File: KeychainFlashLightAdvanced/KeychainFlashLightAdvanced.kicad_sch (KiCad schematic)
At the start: 4 parts, among them SW1 SW_DPST_x2

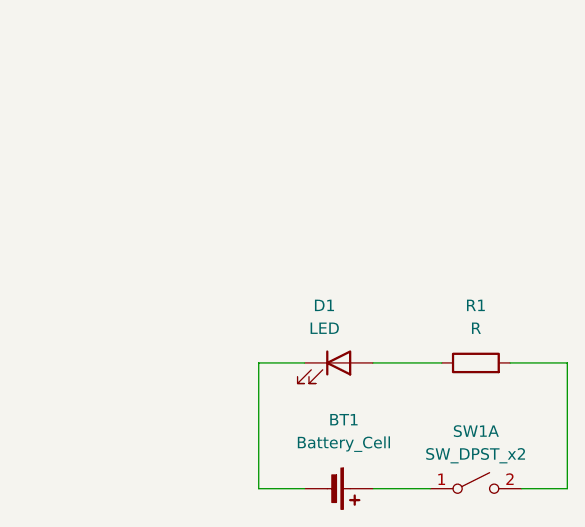
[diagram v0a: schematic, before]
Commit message: Added workshop components
-Add information to the schematic page
-Add informative text to the schematic sheet
-Adding a hierarchical sheet
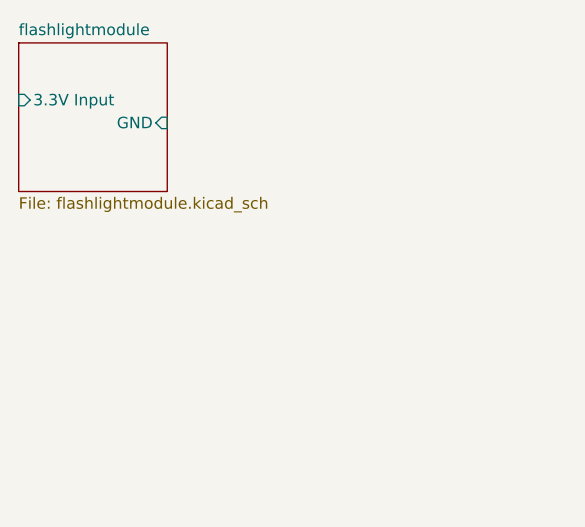
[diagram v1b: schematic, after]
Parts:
- removed BT1: Battery_Cell, Battery:BatteryHolder_Keystone_3002_1x2032, symbol Device:Battery_Cell
- removed D1: LED, LED_THT:LED_D5.0mm_Clear, symbol Device:LED
- removed R1: R, Resistor_THT:R_Axial_DIN0207_L6.3mm_D2.5mm_P10.16mm_Horizontal, symbol Device:R
- removed SW1: SW_DPST_x2, Button_Switch_THT:SW_Tactile_Straight_KSA0Axx1LFTR, symbol Switch:SW_DPST_x2
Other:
- added sheet flashlightmodule (flashlightmodule.kicad_sch)
- title: (none) -> KeychainFlashlightAdvanced
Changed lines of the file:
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@@
 (kicad_sch (version 20230121) (generator eeschema)
-  (paper "A4")
-  (wire (pts (xy 148.59 91.44) (xy 154.94 91.44))
-    (stroke (width 0) (type default))
+  (paper "A5")
+  (title_block
+    (title "KeychainFlashlightAdvanced")
+    (date "2023-12-30")
+    (rev "V0.1")
+    (comment 1 "Made By: Casper Tak")
   )
-  (wire (pts (xy 120.65 91.44) (xy 120.65 105.41))
-    (stroke (width 0) (type default))
-  )
-  (wire (pts (xy 133.35 105.41) (xy 139.7 105.41))
-    (stroke (width 0) (type default))
-  )
-  (wire (pts (xy 154.94 105.41) (xy 149.86 105.41))
-    (stroke (width 0) (type default))
-  )
-  (wire (pts (xy 125.73 91.44) (xy 120.65 91.44))
-    (stroke (width 0) (type default))
-  )
-  (wire (pts (xy 154.94 91.44) (xy 154.94 105.41))
-    (stroke (width 0) (type default))
-  )
-  (wire (pts (xy 133.35 91.44) (xy 140.97 91.44))
-    (stroke (width 0) (type default))
-  )
-  (wire (pts (xy 120.65 105.41) (xy 125.73 105.41))
-    (stroke (width 0) (type default))
-  )
-  (symbol (lib_id "Switch:SW_DPST_x2") (at 144.78 105.41 0) (unit 1)
-    (in_bom yes) (on_board yes) (dnp no) (fields_autoplaced)
-    (property "Reference" "SW1" (at 144.78 99.06 0)
-      (effects (font (size 1.27 1.27)))
+  (sheet (at 93.98 55.88) (size 16.51 16.51) (fields_autoplaced)
+    (stroke (width 0.1524) (type solid))
+    (fill (color 0 0 0 0.0000))
+    (property "Sheetname" "flashlightmodule" (at 93.98 55.1684 0)
+      (effects (font (size 1.27 1.27)) (justify left bottom))
     )
-    (property "Value" "SW_DPST_x2" (at 144.78 101.6 0)
-      (effects (font (size 1.27 1.27)))
+    (property "Sheetfile" "flashlightmodule.kicad_sch" (at 93.98 72.9746 0)
+      (effects (font (size 1.27 1.27)) (justify left top))
     )
-    (property "Footprint" "Button_Switch_THT:SW_Tactile_Straight_KSA0Axx1LFTR" (at 144.78 105.41 0)
-      (effects (font (size 1.27 1.27)) hide)
+    (pin "GND" input (at 110.49 64.77 0)
+      (effects (font (size 1.27 1.27)) (justify right))
     )
-    (property "Datasheet" "~" (at 144.78 105.41 0)
-      (effects (font (size 1.27 1.27)) hide)
+    (pin "3.3V Input" input (at 93.98 62.23 180)
+      (effects (font (size 1.27 1.27)) (justify left))
     )
-    (pin "1")
-    (pin "2")
-    (pin "3")
-    (pin "4")
     (instances
-      (project "KeychainFlashLight"
-        (path "/30398b8a-8fed-4ca8-b3cc-b1f61d914000"
-          (reference "SW1") (unit 1)
-        )
+      (project "KeychainFlashLightAdvanced"
+        (path "/30398b8a-8fed-4ca8-b3cc-b1f61d914000" (page "2"))
       )
     )
-  )
-  (symbol (lib_id "Device:R") (at 144.78 91.44 90) (unit 1)
-    (in_bom yes) (on_board yes) (dnp no) (fields_autoplaced)
-    (property "Reference" "R1" (at 144.78 85.09 90)
-      (effects (font (size 1.27 1.27)))
-    )
-    (property "Value" "R" (at 144.78 87.63 90)
-      (effects (font (size 1.27 1.27)))
-    )
-    (property "Footprint" "Resistor_THT:R_Axial_DIN0207_L6.3mm_D2.5mm_P10.16mm_Horizontal" (at 144.78 93.218 90)
-      (effects (font (size 1.27 1.27)) hide)
-    )
-    (property "Datasheet" "~" (at 144.78 91.44 0)
-      (effects (font (size 1.27 1.27)) hide)
-    )
-    (pin "1")
-    (pin "2")
-    (instances
-      (project "KeychainFlashLight"
-        (path "/30398b8a-8fed-4ca8-b3cc-b1f61d914000"
-          (reference "R1") (unit 1)
-        )
-      )
-    )
-  )
-  (symbol (lib_id "Device:LED") (at 129.54 91.44 0) (unit 1)
-    (in_bom yes) (on_board yes) (dnp no) (fields_autoplaced)
-    (property "Reference" "D1" (at 127.9525 85.09 0)
-      (effects (font (size 1.27 1.27)))
-    )
-    (property "Value" "LED" (at 127.9525 87.63 0)
-      (effects (font (size 1.27 1.27)))
-    )
-    (property "Footprint" "LED_THT:LED_D5.0mm_Clear" (at 129.54 91.44 0)
-      (effects (font (size 1.27 1.27)) hide)
-    )
-    (property "Datasheet" "~" (at 129.54 91.44 0)
-      (effects (font (size 1.27 1.27)) hide)
-    )
-    (pin "1")
-    (pin "2")
-    (instances
-      (project "KeychainFlashLight"
-        (path "/30398b8a-8fed-4ca8-b3cc-b1f61d914000"
-          (reference "D1") (unit 1)
-        )
-      )
-    )
-  )
-  (symbol (lib_id "Device:Battery_Cell") (at 128.27 105.41 270) (unit 1)
-    (in_bom yes) (on_board yes) (dnp no) (fields_autoplaced)
-    (property "Reference" "BT1" (at 130.1115 97.79 90)
-      (effects (font (size 1.27 1.27)))
-    )
-    (property "Value" "Battery_Cell" (at 130.1115 100.33 90)
-      (effects (font (size 1.27 1.27)))
-    )
-    (property "Footprint" "Battery:BatteryHolder_Keystone_3002_1x2032" (at 129.794 105.41 90)
-      (effects (font (size 1.27 1.27)) hide)
-    )
-    (property "Datasheet" "~" (at 129.794 105.41 90)
-      (effects (font (size 1.27 1.27)) hide)
-    )
-    (pin "1")
-    (pin "2")
-    (instances
-      (project "KeychainFlashLight"
-        (path "/30398b8a-8fed-4ca8-b3cc-b1f61d914000"
-          (reference "BT1") (unit 1)
-        )
-      )
-    )
